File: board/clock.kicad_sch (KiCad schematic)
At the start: 0 parts

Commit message: add: Hierarchical Sheets
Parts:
- added C1, C2: 10n, Capacitor_SMD:C_0603_1608Metric, symbol Device:C
- added C3: 100n, Capacitor_SMD:C_0603_1608Metric, symbol Device:C
- added R1: 1k, Resistor_SMD:R_0603_1608Metric, symbol Device:R_US
- added R2: 100k, Resistor_SMD:R_0603_1608Metric, symbol Device:R_US
- added RV1: 10k, Potentiometer_THT:Potentiometer_Piher_PT-6-V_Vertical, symbol Device:R_Potentiometer_US
- added SW1, SW2, SW4: SW_SPST, Button_Switch_THT:SW_PUSH_6mm_H4.3mm, symbol Switch:SW_SPST
- added U2: NE555D, Package_SO:SOIC-8_3.9x4.9mm_P1.27mm, symbol Timer:NE555D
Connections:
- new net: C2.2, U2.5 (CV)
- new net: SW1.2 (B), SW2.2 (B), U2.4 (R)
- new net: C1.1, R1.1, RV1.3, U2.2 (TR), U2.7 (DIS)
- new net: R1.2, U2.6 (THR)
- new net 5V: C3.1, R2.1, RV1.1, RV1.2, SW1.1 (A), SW2.1 (A), U2.8 (VCC)
- new net CLOCK: U2.3 (Q)
- new net GND: C1.2, C2.1, C3.2, SW4.2 (B), U2.1 (GND)
- new net RESET: R2.2, SW4.1 (A)
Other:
- note added: "28 k"

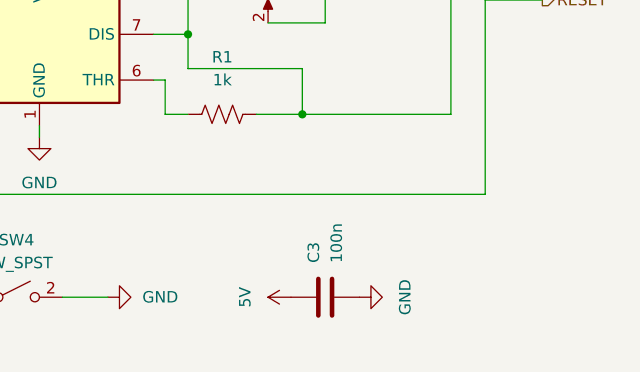
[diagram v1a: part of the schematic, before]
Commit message: add: Mounting holes, box comments
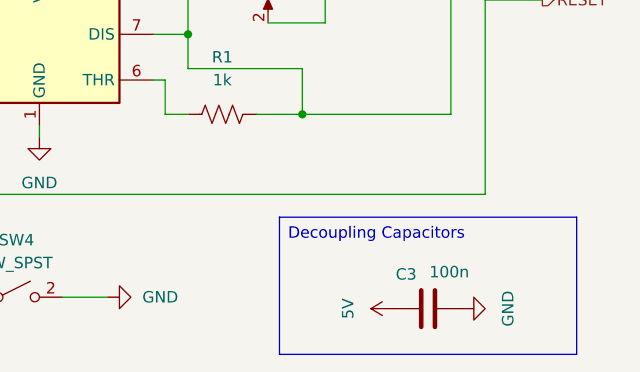
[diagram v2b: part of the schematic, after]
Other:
- moved on the sheet: C3
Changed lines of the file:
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@@
+		)
+	)
+	(text_box "Decoupling Capacitors\n"
+		(exclude_from_sim no)
+		(at 92.71 66.04 0)
+		(size 33.02 15.24)
+		(margins 0.9525 0.9525 0.9525 0.9525)
+		(stroke
+			(width 0)
+			(type solid)
+		)
+		(fill
+			(type none)
+		)
+		(effects
+			(font
+				(size 1.27 1.27)
+			)
+			(justify left top)
 		)
 	)
@@
 	(symbol
 		(lib_id "Device:C")
-		(at 97.79 74.93 90)
+		(at 109.22 76.2 90)
 		(unit 1)
 		(exclude_from_sim no)
@@
 		(on_board yes)
 		(dnp no)
-		(fields_autoplaced yes)
 		(property "Reference" "C3"
-			(at 96.5199 71.12 0)
+			(at 107.9499 72.39 90)
 			(effects
 				(font
@@
 		)
 		(property "Value" "100n"
-			(at 99.0599 71.12 0)
+			(at 113.792 72.136 90)
 			(effects
 				(font
@@
 		)
 		(property "Footprint" "Capacitor_SMD:C_0603_1608Metric"
-			(at 101.6 73.9648 0)
+			(at 113.03 75.2348 0)
 			(effects
 				(font
@@
 		)
 		(property "Datasheet" "~"
-			(at 97.79 74.93 0)
+			(at 109.22 76.2 0)
 			(effects
 				(font
@@
 		)
 		(property "Description" "Unpolarized capacitor"
-			(at 97.79 74.93 0)
+			(at 109.22 76.2 0)
 			(effects
 				(font
@@
 	(symbol
 		(lib_id "power:GND")
-		(at 101.6 74.93 90)
+		(at 113.03 76.2 90)
 		(unit 1)
 		(exclude_from_sim no)
@@
 		(fields_autoplaced yes)
 		(property "Reference" "#PWR010"
-			(at 107.95 74.93 0)
+			(at 119.38 76.2 0)
 			(effects
 				(font
@@
 		)
 		(property "Value" "GND"
-			(at 106.68 74.93 0)
+			(at 118.11 76.2 0)
 			(effects
 				(font
@@
 		)
 		(property "Footprint" ""
-			(at 101.6 74.93 0)
+			(at 113.03 76.2 0)
 			(effects
 				(font
@@
 		)
 		(property "Datasheet" ""
-			(at 101.6 74.93 0)
+			(at 113.03 76.2 0)
 			(effects
 				(font
@@
 		)
 		(property "Description" "Power symbol creates a global label with name \"GND\" , ground"
-			(at 101.6 74.93 0)
+			(at 113.03 76.2 0)
 			(effects
 				(font
@@
 	(symbol
 		(lib_id "power:VCC")
-		(at 93.98 74.93 90)
+		(at 105.41 76.2 90)
 		(unit 1)
 		(exclude_from_sim no)
@@
 		(fields_autoplaced yes)
 		(property "Reference" "#PWR024"
-			(at 97.79 74.93 0)
+			(at 109.22 76.2 0)
 			(effects
 				(font
@@
 		)
 		(property "Value" "5V"
-			(at 88.9 74.93 0)
+			(at 100.33 76.2 0)
 			(effects
 				(font
@@
 		)
 		(property "Footprint" ""
-			(at 93.98 74.93 0)
+			(at 105.41 76.2 0)
 			(effects
 				(font
@@
 		)
 		(property "Datasheet" ""
-			(at 93.98 74.93 0)
+			(at 105.41 76.2 0)
 			(effects
 				(font
@@
 		)
 		(property "Description" "Power symbol creates a global label with name \"VCC\""
-			(at 93.98 74.93 0)
-			(effects
-				(font
+			(at 105.41 76.2 0)
+			(effects
+				(font
